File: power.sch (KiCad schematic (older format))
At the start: 23 parts, among them J10 Jack-DC, J11 USB_B_Micro, U11 AZ2940-5.0, U12 MAX40203AUK, U13 LP2985-3.3, U14 MAX40203AUK

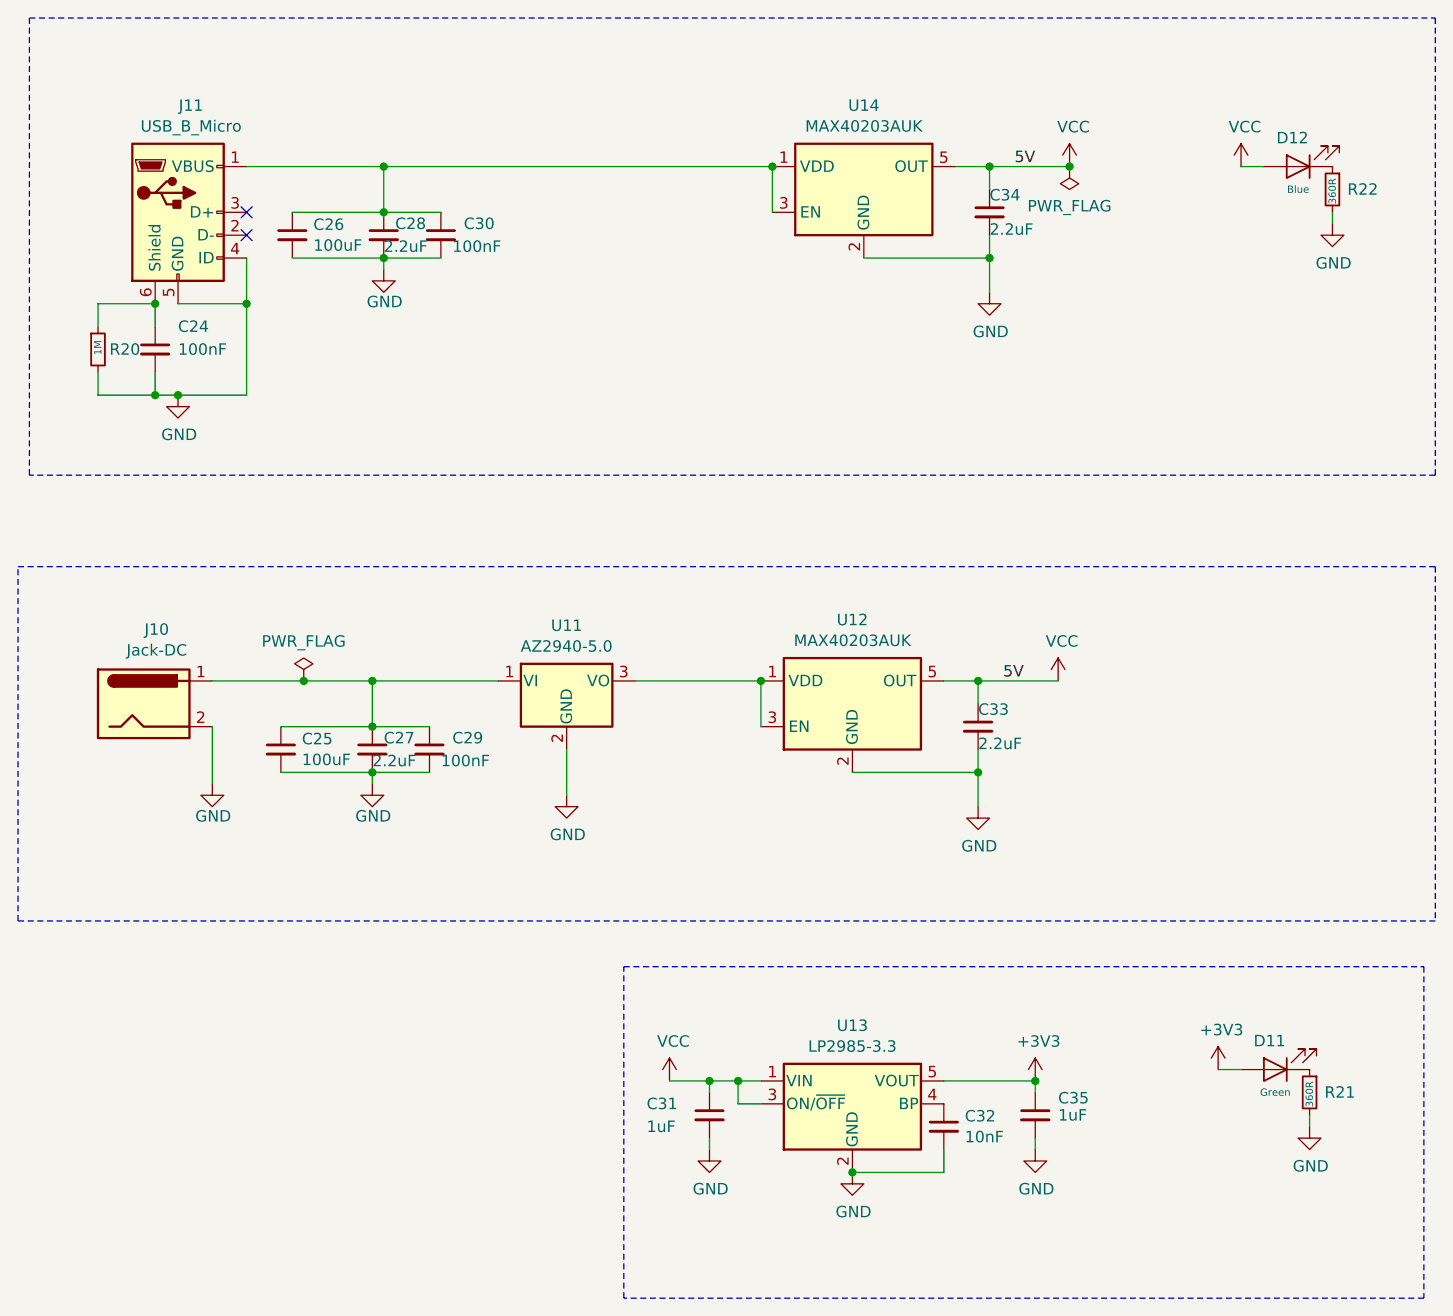
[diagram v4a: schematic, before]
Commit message: Changed 5V regulator, added additional SS text
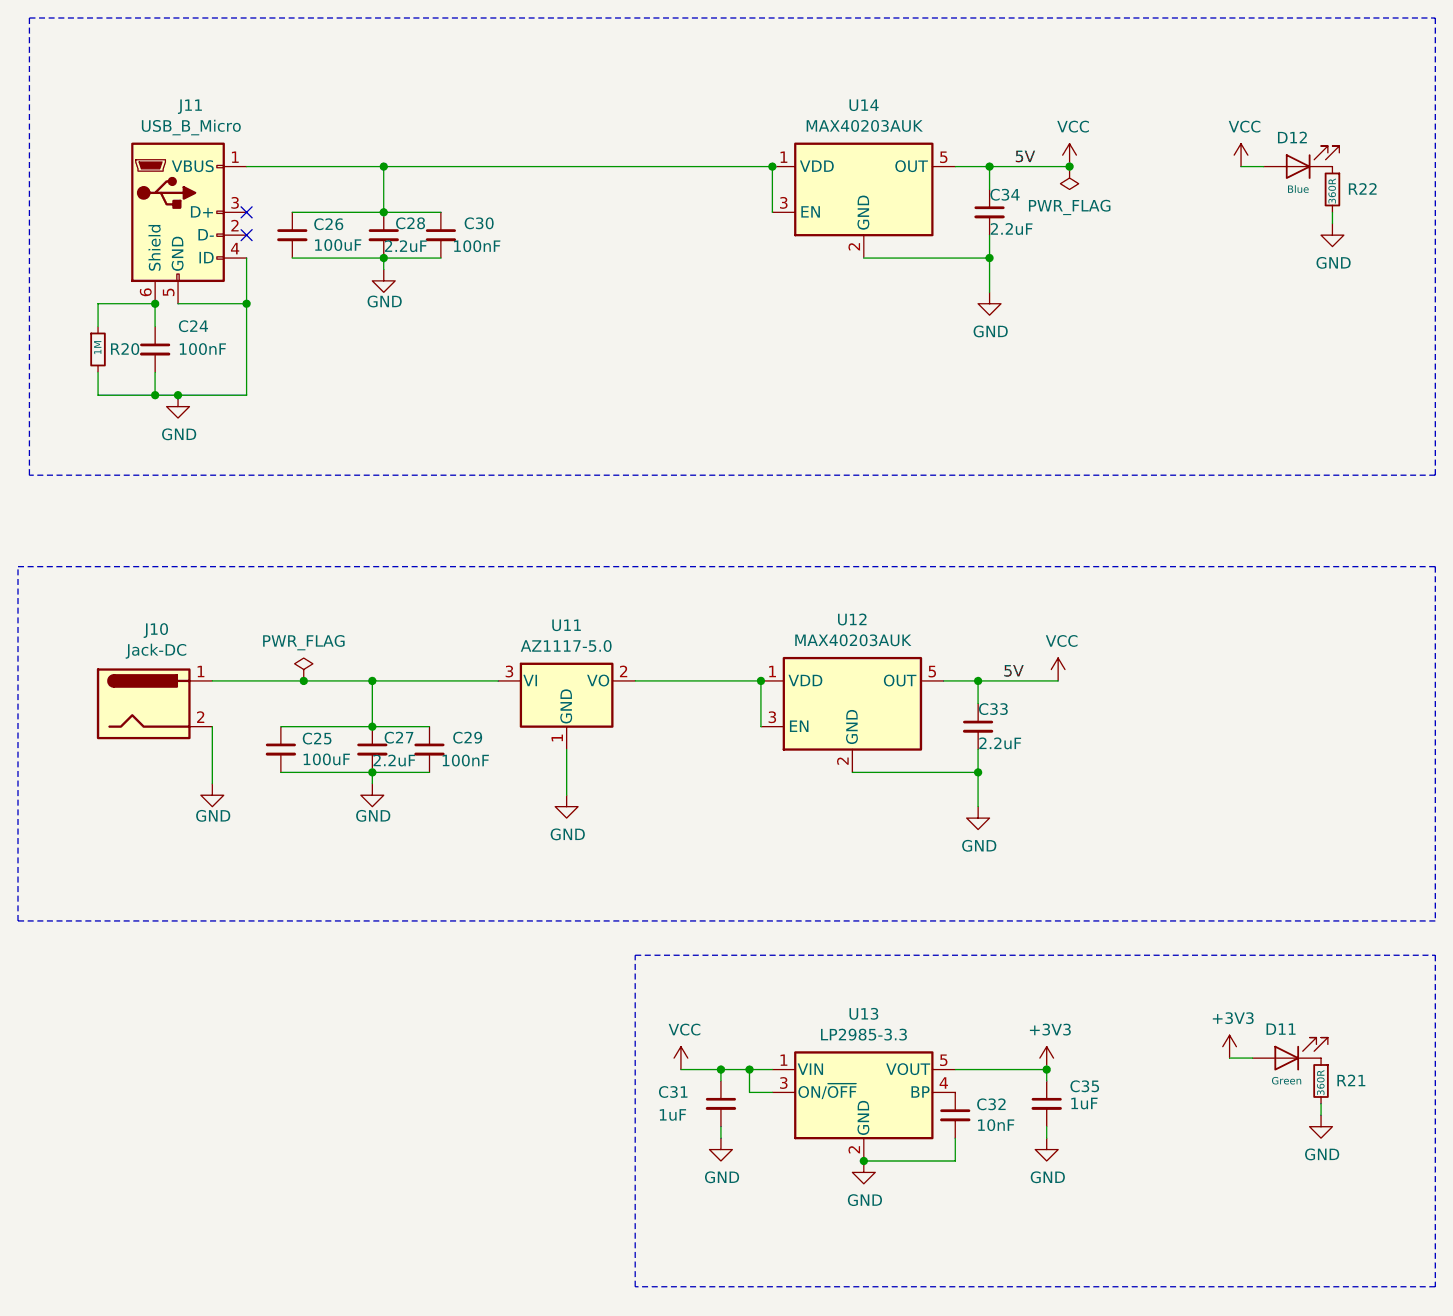
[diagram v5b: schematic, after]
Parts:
- removed U11: AZ2940-5.0, Package_TO_SOT_SMD:TO-252-2, symbol Regulator_Linear:AZ2940-5.0
- added U11: AZ1117-5.0, Package_TO_SOT_SMD:TO-252-3_TabPin2, symbol Regulator_Linear:AZ1117-5.0
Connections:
- net GND: now also U11.1 (GND)
- net at C25.1, C27.1, C29.1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: now also U11.3 (VI)
- net at U12.1 (VDD), U12.3 (EN): now also U11.2 (VO)
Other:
- moved on the sheet: C31, C32, C35, D11, R21, U13
